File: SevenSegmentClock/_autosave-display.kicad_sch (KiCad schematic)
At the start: 86 parts, among them Q1 PN2222A, Q2 PN2222A, Q3 PN2222A, Q4 PN2222A, U1 4504, U10 4511, U2 74HC138, U3 4504, U4 4042, U5 4511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

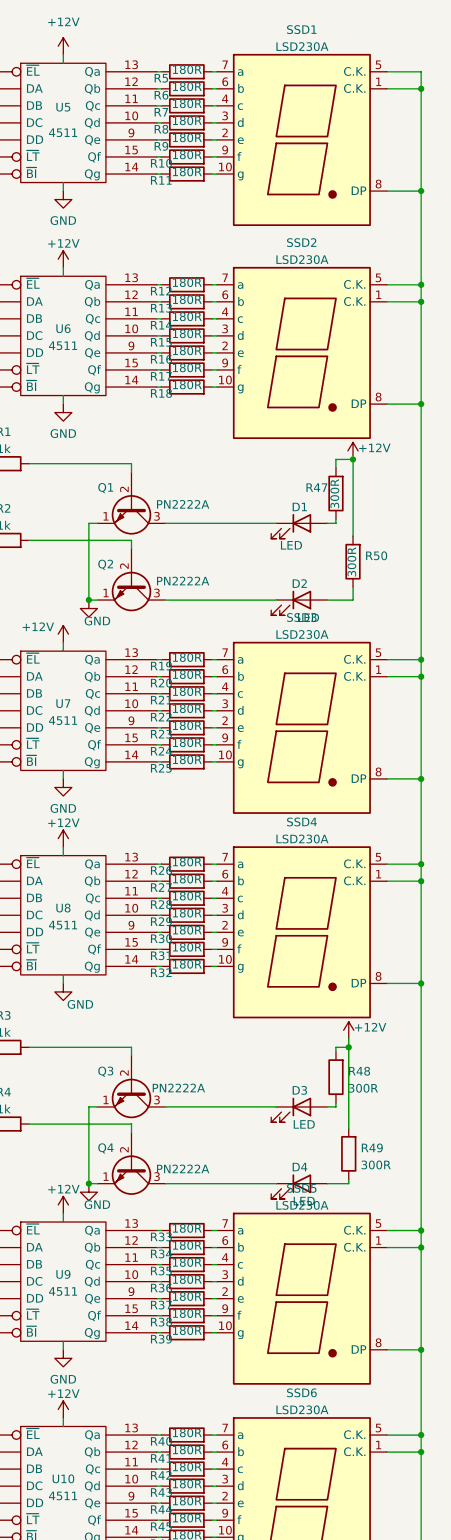
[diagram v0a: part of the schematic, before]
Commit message: Modifying code to use direct port manipulation
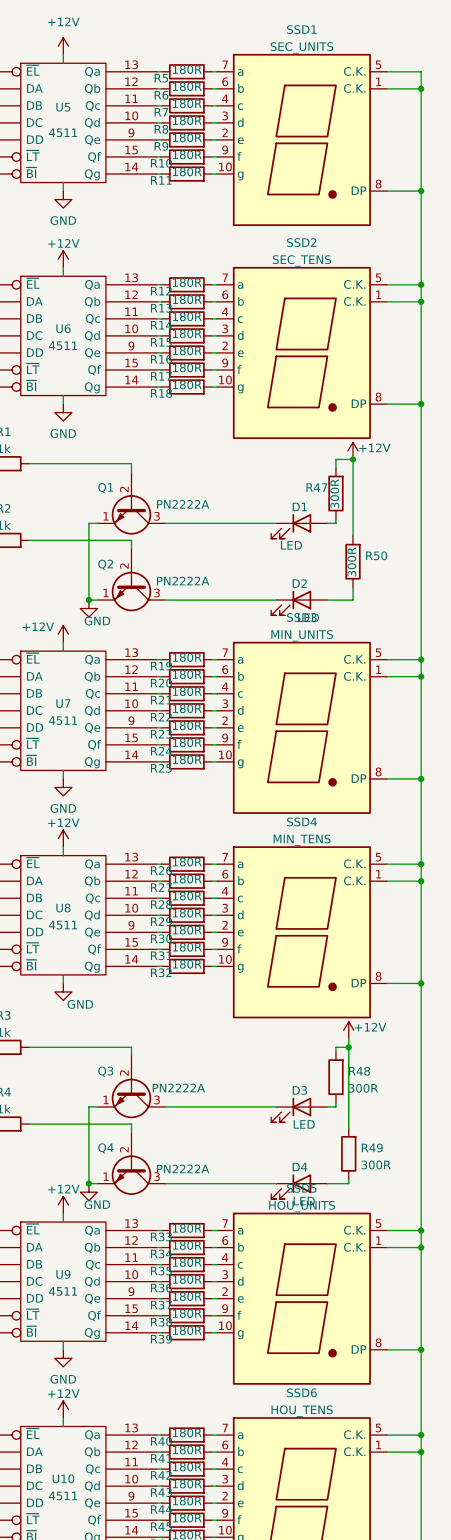
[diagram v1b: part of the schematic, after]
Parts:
- SSD1: value LSD230A -> SEC_UNITS
- SSD2: value LSD230A -> SEC_TENS
- SSD3: value LSD230A -> MIN_UNITS
- SSD4: value LSD230A -> MIN_TENS
- SSD5: value LSD230A -> HOU_UNITS
- SSD6: value LSD230A -> HOU_TENS
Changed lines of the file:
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@@
     (in_bom yes) (on_board yes) (fields_autoplaced)
     (property "Reference" "SSD6" (id 0) (at 162.56 217.2802 0))
-    (property "Value" "LSD230A" (id 1) (at 162.56 219.8171 0))
+    (property "Value" "HOU_TENS" (id 1) (at 162.56 219.8171 0))
     (property "Footprint" "Library:LSD230A" (id 2) (at 163.83 233.68 0)
       (effects (font (size 1.27 1.27)) hide)
@@
     (in_bom yes) (on_board yes) (fields_autoplaced)
     (property "Reference" "SSD1" (id 0) (at 162.56 14.0802 0))
-    (property "Value" "LSD230A" (id 1) (at 162.56 16.6171 0))
+    (property "Value" "SEC_UNITS" (id 1) (at 162.56 16.6171 0))
     (property "Footprint" "Library:LSD230A" (id 2) (at 163.83 30.48 0)
       (effects (font (size 1.27 1.27)) hide)
@@
     (in_bom yes) (on_board yes) (fields_autoplaced)
     (property "Reference" "SSD3" (id 0) (at 162.56 101.7102 0))
-    (property "Value" "LSD230A" (id 1) (at 162.56 104.2471 0))
+    (property "Value" "MIN_UNITS" (id 1) (at 162.56 104.2471 0))
     (property "Footprint" "Library:LSD230A" (id 2) (at 163.83 118.11 0)
       (effects (font (size 1.27 1.27)) hide)
@@
     (in_bom yes) (on_board yes) (fields_autoplaced)
     (property "Reference" "SSD2" (id 0) (at 162.56 45.8302 0))
-    (property "Value" "LSD230A" (id 1) (at 162.56 48.3671 0))
+    (property "Value" "SEC_TENS" (id 1) (at 162.56 48.3671 0))
     (property "Footprint" "Library:LSD230A" (id 2) (at 163.83 62.23 0)
       (effects (font (size 1.27 1.27)) hide)
@@
     (in_bom yes) (on_board yes) (fields_autoplaced)
     (property "Reference" "SSD4" (id 0) (at 162.56 132.1902 0))
-    (property "Value" "LSD230A" (id 1) (at 162.56 134.7271 0))
+    (property "Value" "MIN_TENS" (id 1) (at 162.56 134.7271 0))
     (property "Footprint" "Library:LSD230A" (id 2) (at 163.83 148.59 0)
       (effects (font (size 1.27 1.27)) hide)
@@
     (in_bom yes) (on_board yes) (fields_autoplaced)
     (property "Reference" "SSD5" (id 0) (at 162.56 186.8002 0))
-    (property "Value" "LSD230A" (id 1) (at 162.56 189.3371 0))
+    (property "Value" "HOU_UNITS" (id 1) (at 162.56 189.3371 0))
     (property "Footprint" "Library:LSD230A" (id 2) (at 163.83 203.2 0)
       (effects (font (size 1.27 1.27)) hide)
